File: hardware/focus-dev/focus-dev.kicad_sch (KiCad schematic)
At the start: 2 parts

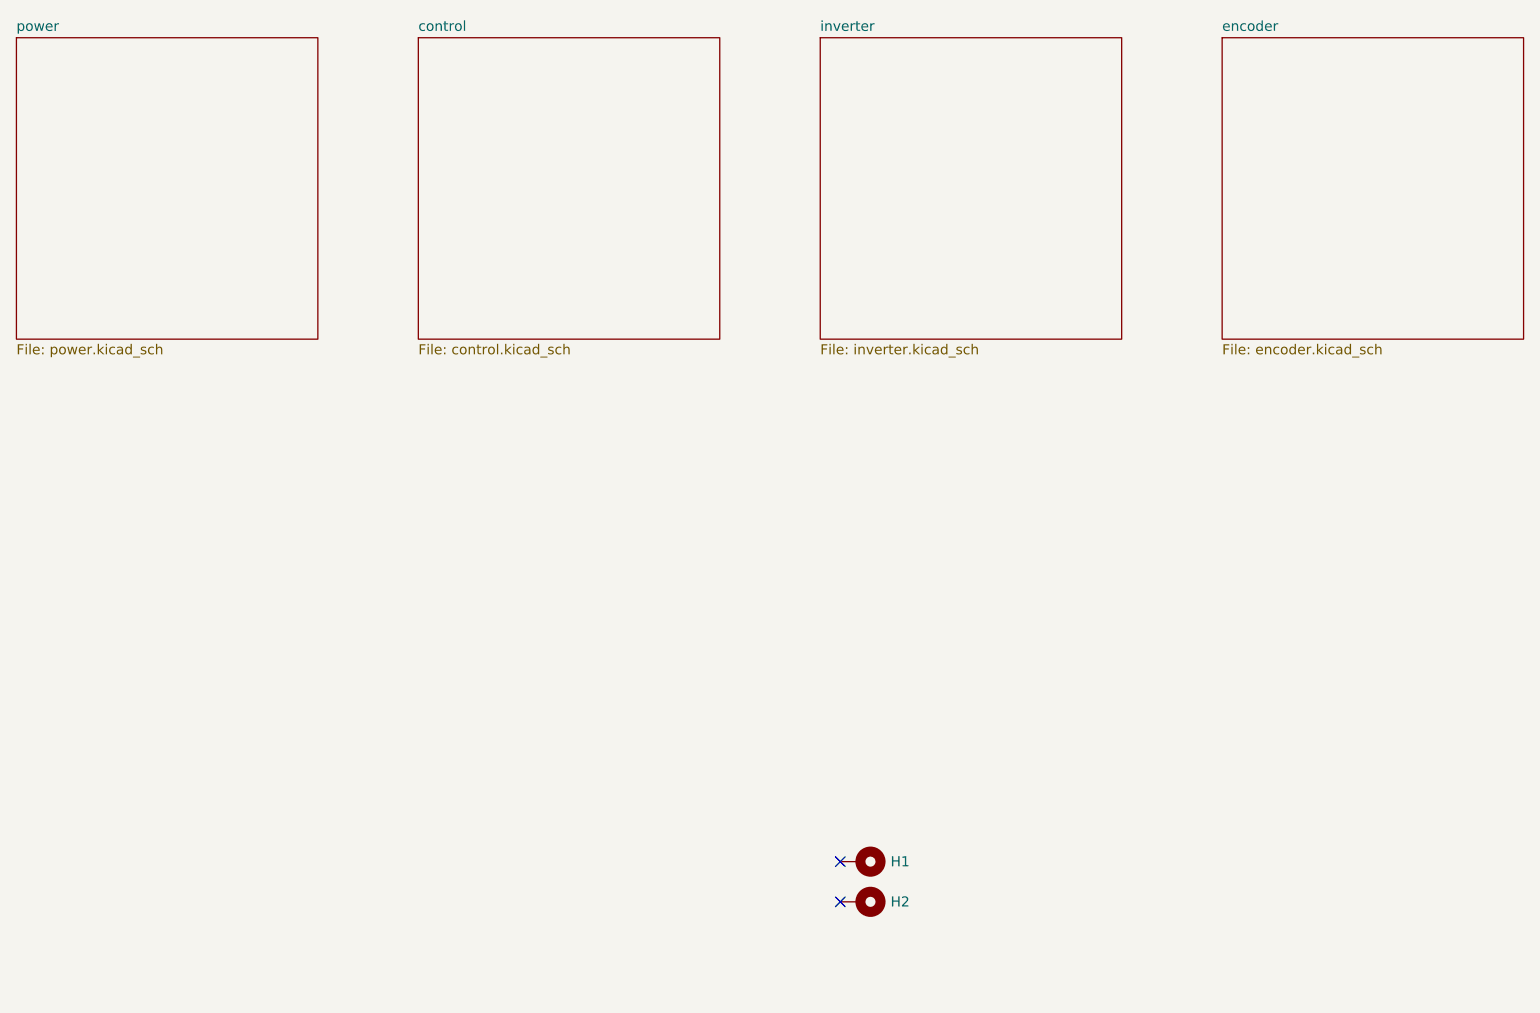
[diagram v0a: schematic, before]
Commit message: wip: remove onboard encoders
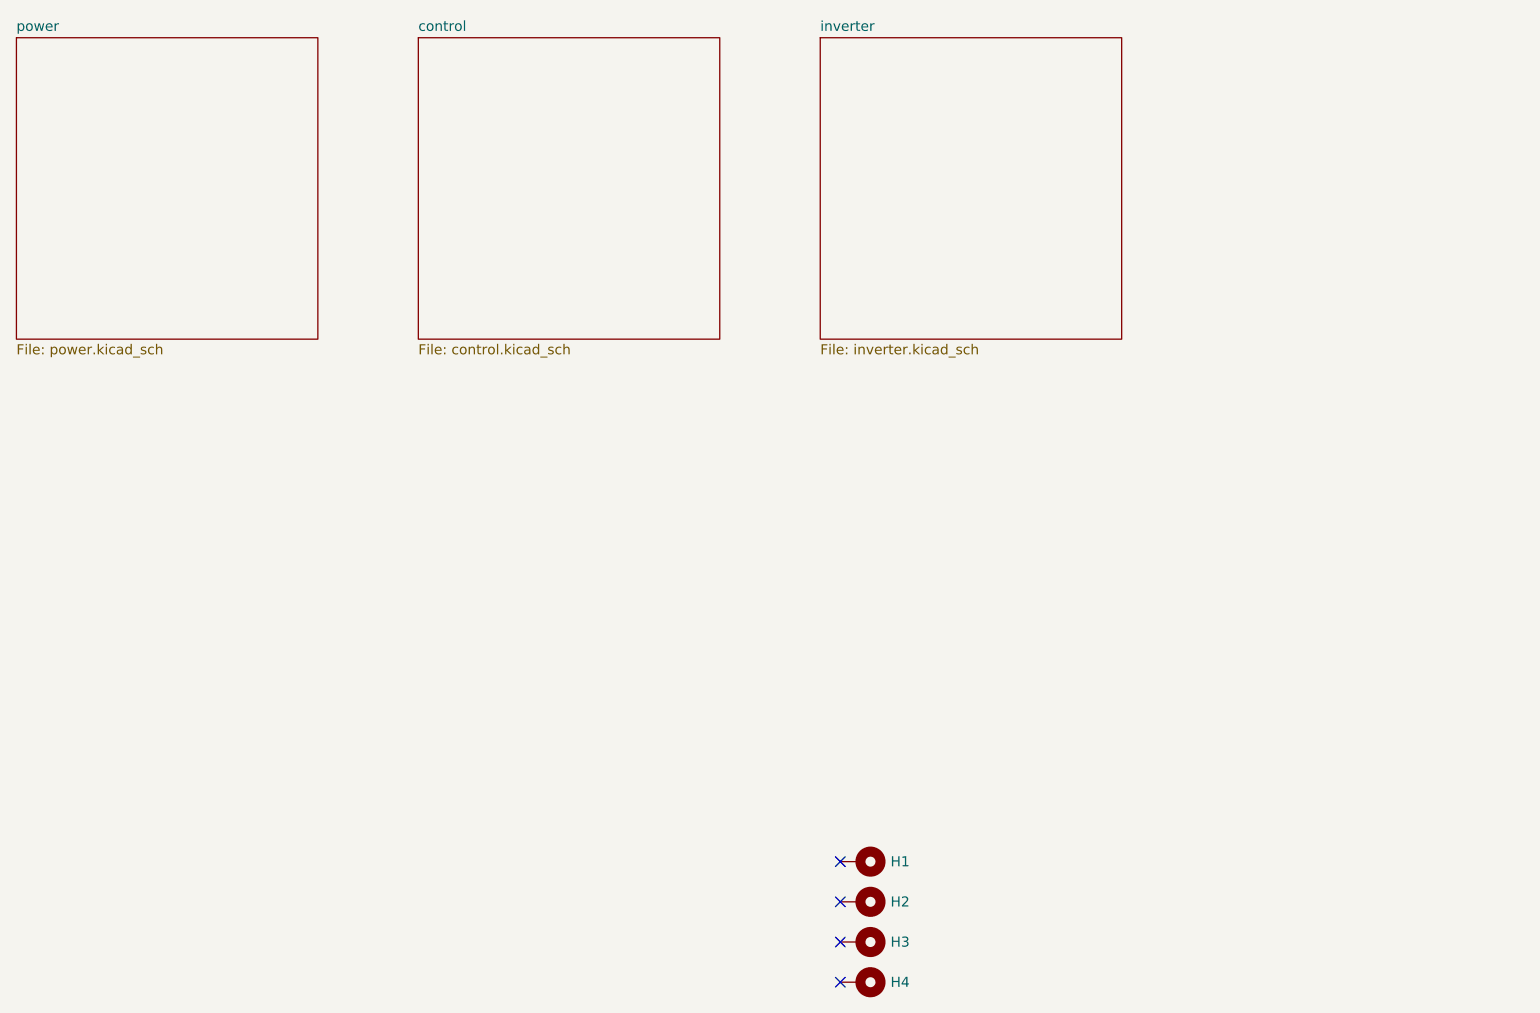
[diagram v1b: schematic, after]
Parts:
- added H3, H4: MountingHole_Pad, MountingHole:MountingHole_3.2mm_M3_Pad_Via, symbol Mechanical:MountingHole_Pad
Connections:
- no-connect marks 2 -> 4
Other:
- removed sheet encoder
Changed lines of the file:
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@@
+	)
+	(no_connect
+		(at 154.94 182.88)
 	)
 	(no_connect
 		(at 154.94 167.64)
 	)
+	(no_connect
+		(at 154.94 177.8)
+	)
+	(symbol
+		(lib_id "Mechanical:MountingHole_Pad")
+		(at 157.48 177.8 270)
+		(unit 1)
+		(exclude_from_sim no)
+		(in_bom no)
+		(on_board yes)
+		(dnp no)
+		(fields_autoplaced yes)
+		(property "Reference" "H3"
+			(at 161.29 177.7999 90)
+			(effects
+				(font
+					(size 1.27 1.27)
+				)
+				(justify left)
+			)
+		)
+		(property "Value" "MountingHole_Pad"
+			(at 161.29 179.0699 90)
+			(effects
+				(font
+					(size 1.27 1.27)
+				)
+				(justify left)
+				(hide yes)
+			)
+		)
+		(property "Footprint" "MountingHole:MountingHole_3.2mm_M3_Pad_Via"
+			(at 157.48 177.8 0)
+			(effects
+				(font
+					(size 1.27 1.27)
+				)
+				(hide yes)
+			)
+		)
+		(property "Datasheet" "~"
+			(at 157.48 177.8 0)
+			(effects
+				(font
+					(size 1.27 1.27)
+				)
+				(hide yes)
+			)
+		)
+		(property "Description" "Mounting Hole with connection"
+			(at 157.48 177.8 0)
+			(effects
+				(font
+					(size 1.27 1.27)
+				)
+				(hide yes)
+			)
+		)
+		(pin "1"
+		)
+		(instances
+			(project "focus-dev"
+				(path "/2dd819a8-72e5-4f85-99df-ac0fc9d47246"
+					(reference "H3")
+					(unit 1)
+				)
+			)
+		)
+	)
 	(symbol
 		(lib_id "Mechanical:MountingHole_Pad")
@@
 		)
 	)
-	(sheet
-		(at 203.2 63.5)
-		(size 38.1 38.1)
-		(exclude_from_sim no)
-		(in_bom yes)
-		(on_board yes)
-		(dnp no)
-		(fields_autoplaced yes)
-		(stroke
-			(width 0.1524)
-			(type solid)
-		)
-		(fill
-			(color 0 0 0 0.0000)
-		)
-		(property "Sheetname" "encoder"
-			(at 203.2 62.7884 0)
-			(effects
-				(font
-					(size 1.27 1.27)
-				)
-				(justify left bottom)
-			)
-		)
-		(property "Sheetfile" "encoder.kicad_sch"
-			(at 203.2 102.1846 0)
-			(effects
-				(font
-					(size 1.27 1.27)
-				)
-				(justify left top)
-			)
+	(symbol
+		(lib_id "Mechanical:MountingHole_Pad")
+		(at 157.48 182.88 270)
+		(unit 1)
+		(exclude_from_sim no)
+		(in_bom no)
+		(on_board yes)
+		(dnp no)
+		(fields_autoplaced yes)
+		(property "Reference" "H4"
+			(at 161.29 182.8799 90)
+			(effects
+				(font
+					(size 1.27 1.27)
+				)
+				(justify left)
+			)
+		)
+		(property "Value" "MountingHole_Pad"
+			(at 161.29 184.1499 90)
+			(effects
+				(font
+					(size 1.27 1.27)
+				)
+				(justify left)
+				(hide yes)
+			)
+		)
+		(property "Footprint" "MountingHole:MountingHole_3.2mm_M3_Pad_Via"
+			(at 157.48 182.88 0)
+			(effects
+				(font
+					(size 1.27 1.27)
+				)
+				(hide yes)
+			)
+		)
+		(property "Datasheet" "~"
+			(at 157.48 182.88 0)
+			(effects
+				(font
+					(size 1.27 1.27)
+				)
+				(hide yes)
+			)
+		)
+		(property "Description" "Mounting Hole with connection"
+			(at 157.48 182.88 0)
+			(effects
+				(font
+					(size 1.27 1.27)
+				)
+				(hide yes)
+			)
+		)
+		(pin "1"
 		)
 		(instances
 			(project "focus-dev"
 				(path "/2dd819a8-72e5-4f85-99df-ac0fc9d47246"
-					(page "4")
-				)
-			)
+					(reference "H4")
+					(unit 1)
+				)
+			)
